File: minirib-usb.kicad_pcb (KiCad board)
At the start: 2 copper layers, 49.5 x 22.5 mm, 48 parts, among them J1 USB_B_Micro, J2 Mini-DIN-6-Shielded, Q1 MMST3904-7-F, Q2 MMST3906-7-F, Q3 MMST3906-7-F, Q4 MMST3904-7-F, Q5 MMST3904-7-F, Q6 MMST3904-7-F, Q7 MMST3904-7-F, U1 FT231XS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

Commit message: converted to Kicad 6 project
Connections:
- net ~BUSY renamed ~{BUSY}
- net ~CTS renamed ~{CTS}
- net ~DTR renamed ~{DTR}
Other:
- net class Default removed

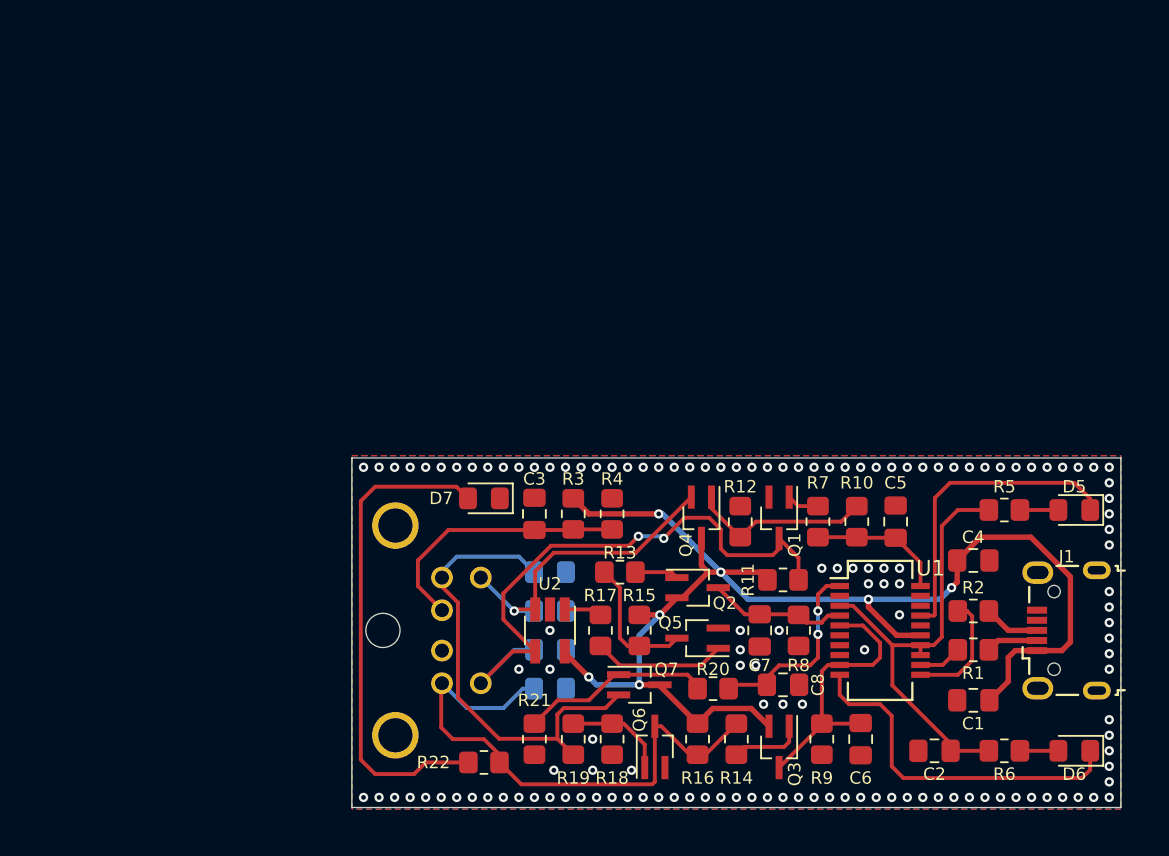
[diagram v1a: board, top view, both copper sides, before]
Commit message: started work on PCB, added LTSpice sims for circuit
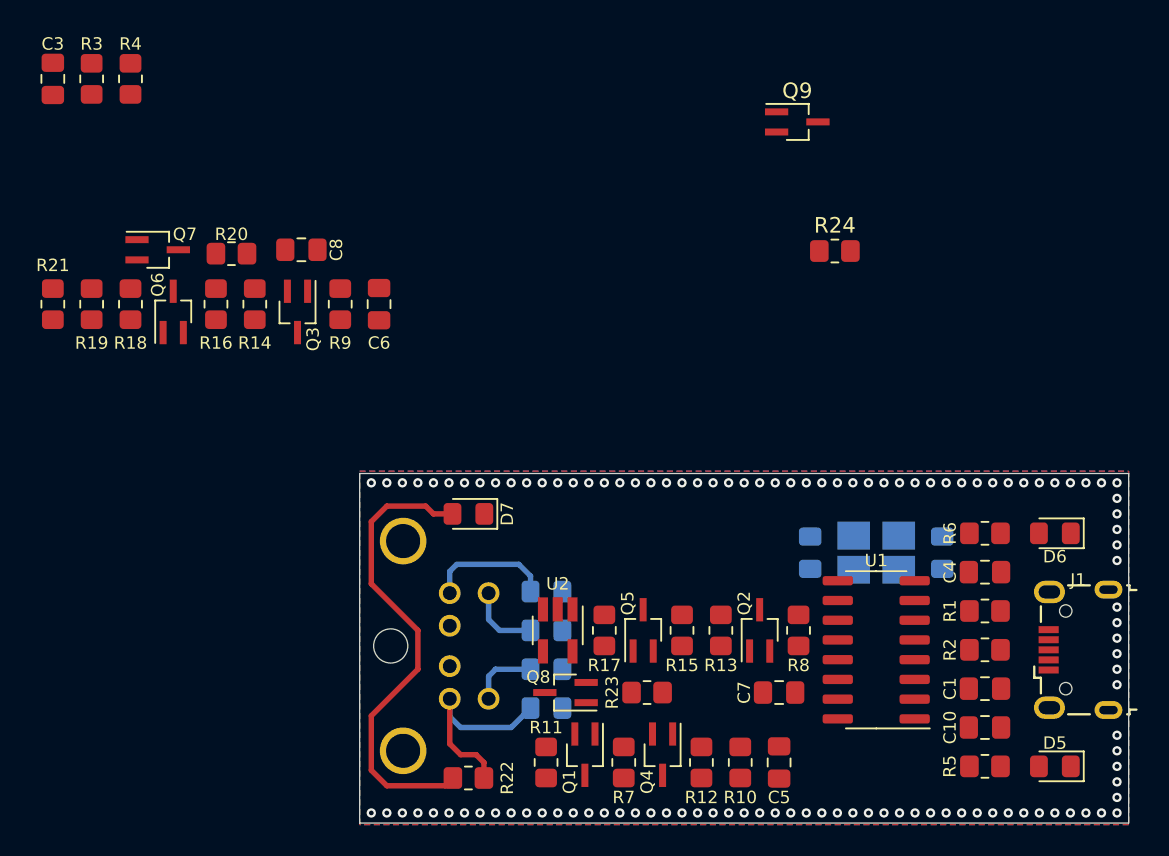
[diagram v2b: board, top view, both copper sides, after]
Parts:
- added C10: 0.1uF, Capacitor_SMD:C_0805_2012Metric_Pad1.18x1.45mm_HandSolder, F.Cu at (163.2, 106.2)
- added C9: 0.1uF, Capacitor_SMD:C_0805_2012Metric_Pad1.18x1.45mm_HandSolder, B.Cu at (160.5, 95.0)
- added Q8: MMST3906-7-F, Package_TO_SOT_SMD:SOT-323_SC-70_Handsoldering, F.Cu at (136.2, 104.0)
- added Q9: MMST3906-7-F, Package_TO_SOT_SMD:SOT-323_SC-70_Handsoldering, F.Cu at (151.2, 67.3)
- added R23: 4k7, Resistor_SMD:R_0805_2012Metric_Pad1.20x1.40mm_HandSolder, F.Cu at (141.5, 104.0)
- added R24: 4k7, Resistor_SMD:R_0805_2012Metric_Pad1.20x1.40mm_HandSolder, F.Cu at (153.6, 75.6)
- added Y1: 12MHz, Crystal:Crystal_SMD_SeikoEpson_FA238-4Pin_3.2x2.5mm_HandSoldering, B.Cu at (156.2, 95.0)
- C2: moved to B.Cu
- J2: value Mini-DIN-6-Shielded -> SB9600 Out
- U1: value FT231XS -> CH340G; footprint Package_SO:SSOP-20_3.9x8.7mm_P0.635mm -> Package_SO:SOIC-16_3.9x9.9mm_P1.27mm
- moved C3 41.8 mm to (103.2, 64.5)
- moved C6 41.8 mm to (124.2, 79.0)
- moved C8 41.8 mm to (119.2, 75.5)
- moved Q3 41.8 mm to (119.0, 79.5)
- moved Q6 41.8 mm to (111.0, 79.5)
- moved Q7 41.8 mm to (110.0, 75.5)
- moved R14 41.8 mm to (116.2, 79.0)
- moved R16 41.8 mm to (113.8, 79.0)
- moved R18 41.8 mm to (108.2, 79.0)
- moved R19 41.8 mm to (105.8, 79.0)
- moved R20 41.8 mm to (114.8, 75.8)
- moved R21 41.8 mm to (103.2, 79.0)
- moved R3 41.8 mm to (105.8, 64.5)
- moved R4 41.8 mm to (108.2, 64.5)
- moved R9 41.8 mm to (121.8, 79.0)
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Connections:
- C2 pad 1: GND -> Net-(C2-Pad1)
- C2 pad 2: +3V3 -> GND
- D3 pad 1: GND -> BUSY
- D3 pad 2: BUSY -> GND
- D4 pad 1: GND -> BUS+
- D4 pad 2: BUS+ -> GND
- D5 pad 1: Net-(D5-Pad1) -> TXD
- D6 pad 1: Net-(D6-Pad1) -> RXD
- J1 pad 2: Net-(J1-Pad2) -> Net-(R2-Pad1)
- J1 pad 3: Net-(J1-Pad3) -> Net-(R1-Pad2)
- J1 pad 4: Net-(J1-Pad4) -> unconnected-(J1-Pad4)
- Q4 pad 2: BUS- -> GND
- Q4 pad 3: +5V -> Net-(Q4-Pad3)
- Q7 pad 2: ~{BUSY} -> GND
- Q7 pad 3: +5V -> Net-(Q7-Pad3)
- R1 pad 2: Net-(J1-Pad2) -> Net-(R1-Pad2)
- R2 pad 1: Net-(J1-Pad3) -> Net-(R2-Pad1)
- R5 pad 1: +3V3 -> +5V
- R6 pad 2: +3V3 -> +5V
- U1 pad 1: ~{DTR} -> GND
- U1 pad 10: Net-(D6-Pad1) -> unconnected-(U1-Pad10)
- U1 pad 11: Net-(R2-Pad2) -> ~{CTS}
- U1 pad 12: Net-(R1-Pad1) -> unconnected-(U1-Pad12)
- U1 pad 13: +3V3 -> ~{DTR}
- U1 pad 14: +3V3 -> unconnected-(U1-Pad14)
- U1 pad 15: +5V -> unconnected-(U1-Pad15)
- U1 pad 16: GND -> +5V
- U1 pad 2: Net-(U1-Pad2) -> TXD
- U1 pad 3: +3V3 -> RXD
- U1 pad 4: RXD -> Net-(C10-Pad1)
- U1 pad 5: ~{CTS} -> Net-(R1-Pad1)
- U1 pad 6: GND -> Net-(R2-Pad2)
- U1 pad 7: Net-(U1-Pad7) -> Net-(C2-Pad1)
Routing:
- net +5V: track 87.7 -> 0.00 mm, vias 7 -> 0
- net BUS+: track 39.1 -> 4.34 mm, vias 2 -> 0
- net +3V3: track 29.9 -> 0.00 mm
- net Net-(D6-Pad1): track 23.0 -> 0.00 mm
- net BUSY: track 36.0 -> 13.8 mm
- net ~{BUSY}: track 30.3 -> 8.10 mm
- net Net-(D5-Pad1): track 20.0 -> 0.00 mm
- net ~{CTS}: track 18.0 -> 0.00 mm
- net BIAS: track 17.2 -> 0.00 mm
- net BUS-: track 20.2 -> 4.69 mm, vias 1 -> 0
- net Net-(Q7-Pad1): track 12.8 -> 0.00 mm
- net ~{DTR}: track 12.4 -> 0.00 mm, vias 2 -> 0
- net Net-(Q4-Pad1): track 11.7 -> 0.00 mm
- net RXD: track 9.04 -> 0.00 mm
- net TXD: track 8.78 -> 0.00 mm
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
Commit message: finalized PCB & schematic for rev B
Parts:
- C3, R3, R4: moved to B.Cu
- moved R21 58.5 mm to (159.2, 95.8), turned to -90 degrees
- moved Q7 49.1 mm to (154.5, 96.2), turned to -90 degrees
- moved R20 46.7 mm to (157.0, 95.8), turned to -90 degrees
- moved R19 44.5 mm to (147.0, 95.8)
- moved C8 41.0 mm to (151.5, 100.8), turned to -90 degrees
- moved R18 40.2 mm to (144.8, 95.8), turned to -90 degrees
- moved C3 39.3 mm to (130.0, 93.2)
- moved R3 39.1 mm to (132.2, 93.2), turned to -90 degrees
- moved R4 38.9 mm to (134.5, 93.2), turned to 90 degrees
- moved Q6 35.3 mm to (142.2, 96.0), turned to -90 degrees
- moved R16 30.9 mm to (139.8, 95.8), turned to -90 degrees
- moved Q9 29.0 mm to (149.5, 96.2), turned to -90 degrees
- moved R14 27.1 mm to (137.5, 95.8)
- moved Q3 23.0 mm to (135.0, 96.0), turned to 90 degrees
- moved C6 21.3 mm to (140.8, 92.5), turned to 0 degrees
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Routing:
- net +5V: track 0.00 -> 127.6 mm, vias 0 -> 1
- net RXD: track 0.00 -> 43.3 mm, vias 0 -> 3
- net TXD: track 0.00 -> 36.8 mm, vias 0 -> 2
- net ~{CTS}: track 0.00 -> 29.4 mm, vias 0 -> 2
- net BUSY: track 13.8 -> 36.8 mm, vias 0 -> 2
- net ~{DTR}: track 0.00 -> 17.5 mm
- net ~{BUSY}: track 8.10 -> 25.1 mm, vias 0 -> 1
- net BUS+: track 4.34 -> 19.9 mm
- net BIAS: track 0.00 -> 13.6 mm
- net Net-(C2-Pad1): track 0.00 -> 12.9 mm, vias 0 -> 1
- net BUS-: track 4.69 -> 16.4 mm
- net Net-(Q4-Pad3): track 0.00 -> 9.80 mm
- net Net-(R1-Pad1): track 0.00 -> 8.42 mm
- net Net-(C9-Pad1): track 0.00 -> 7.02 mm, vias 0 -> 1
- net Net-(Q6-Pad1): track 0.00 -> 5.92 mm
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
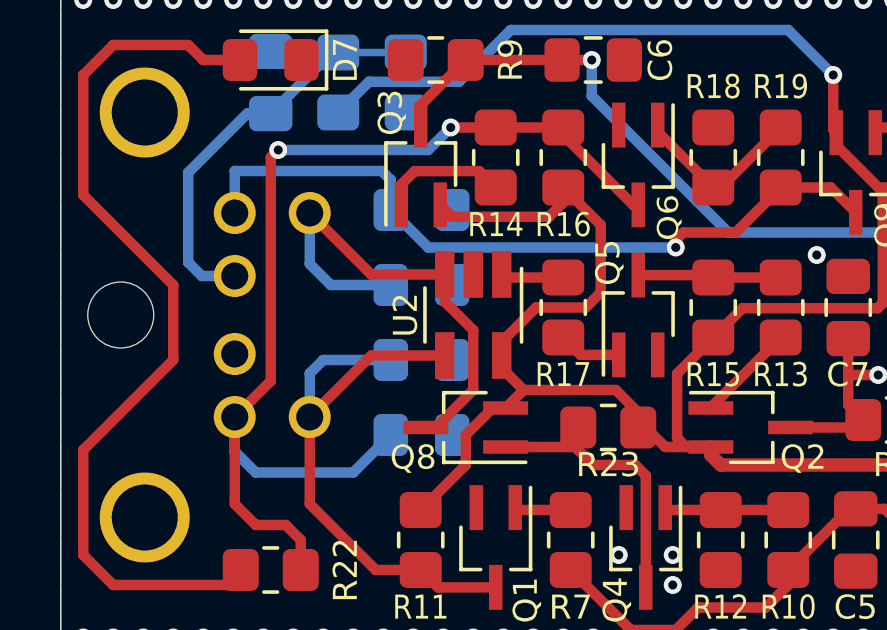
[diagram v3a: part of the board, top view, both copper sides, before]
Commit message: switched to SC70 package for TL081
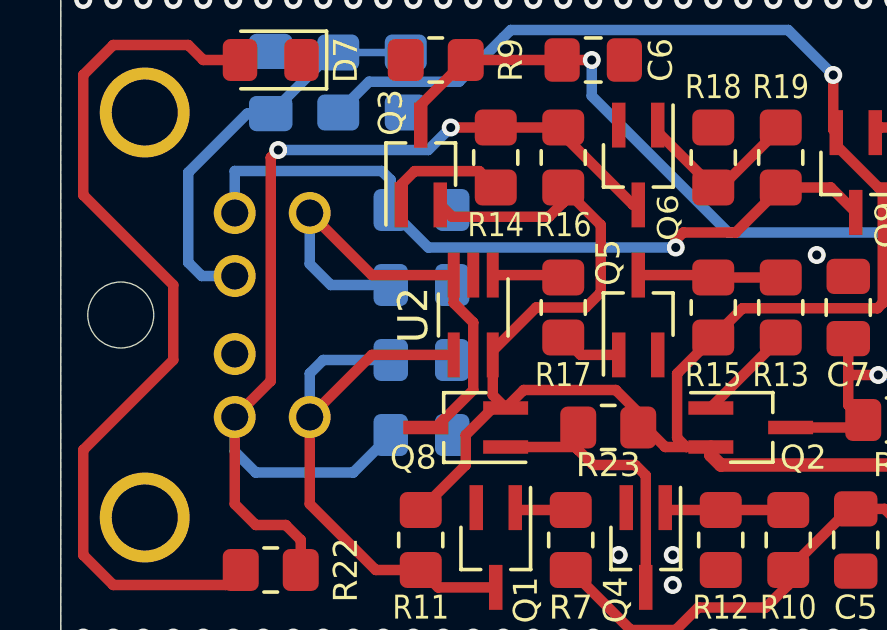
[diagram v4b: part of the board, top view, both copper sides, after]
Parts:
- U2: footprint Package_TO_SOT_SMD:SOT-23-5_HandSoldering -> Package_TO_SOT_SMD:SOT-353_SC-70-5_Handsoldering
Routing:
- net +5V: track 127.6 -> 128.2 mm
